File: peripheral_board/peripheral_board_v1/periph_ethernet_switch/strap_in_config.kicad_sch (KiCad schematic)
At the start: 21 parts, among them J10 Conn_01x03, J11 Conn_01x03, J12 Conn_01x03, J6 Conn_01x03, J7 Conn_01x03, J8 Conn_01x03, J9 Conn_01x03

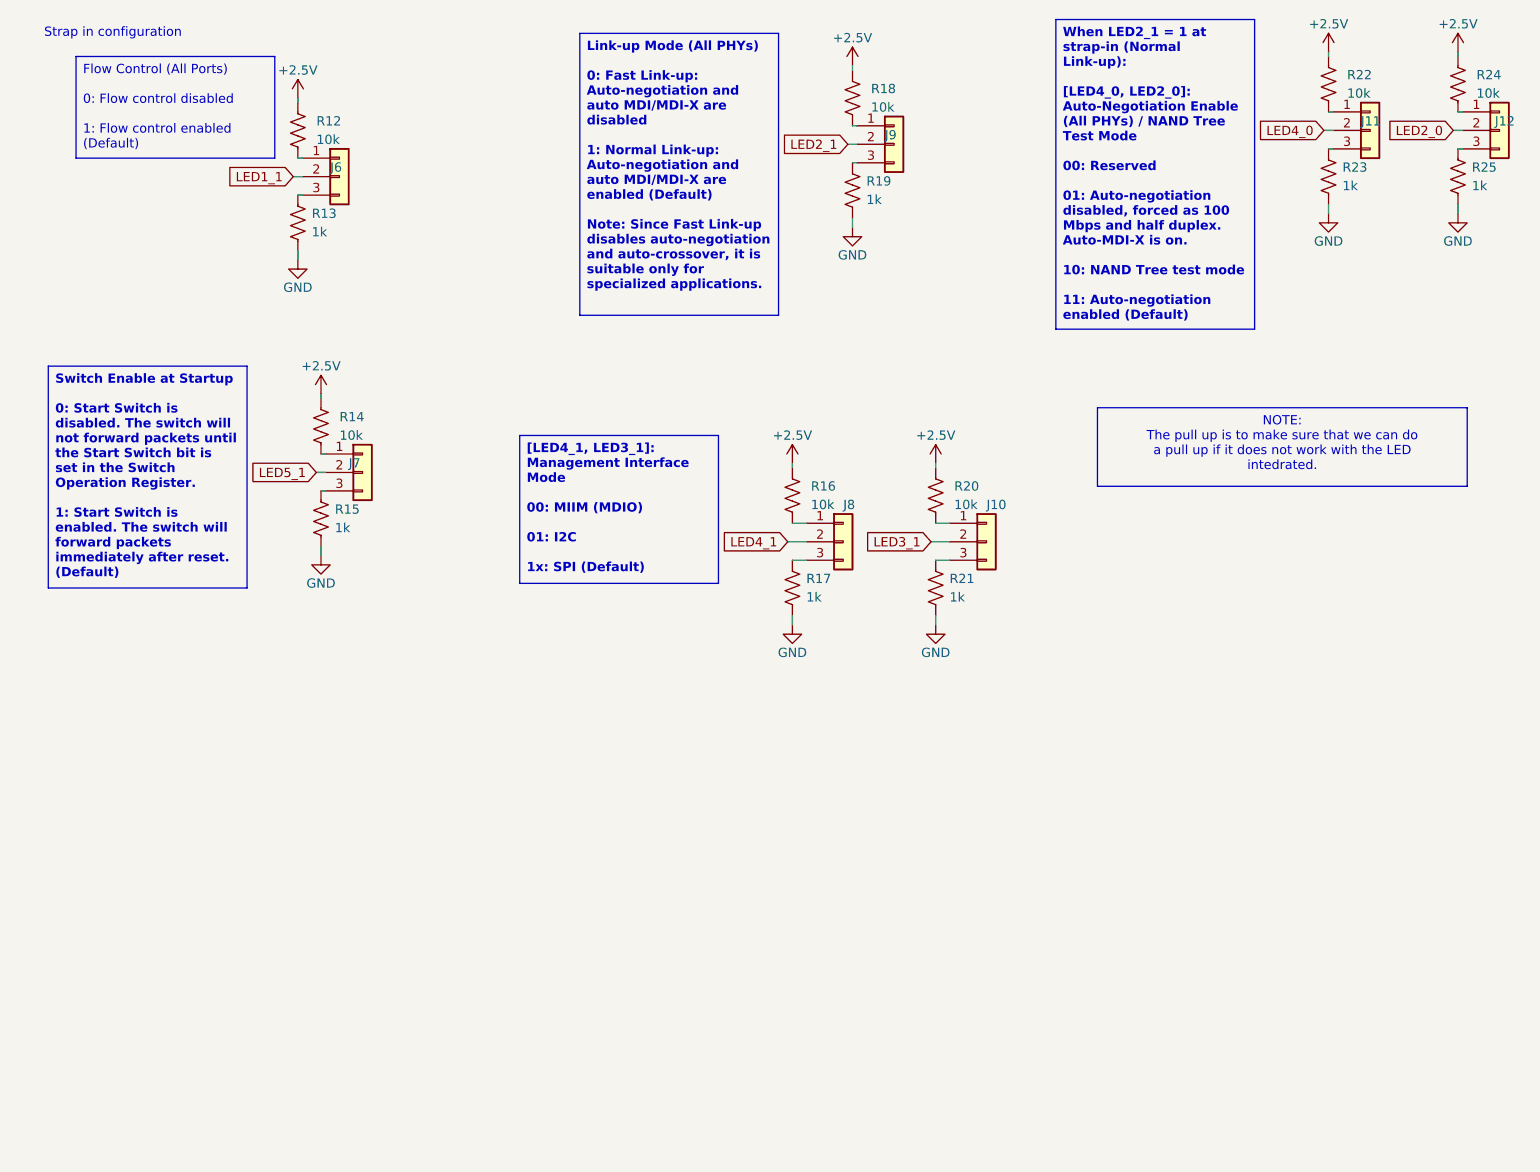
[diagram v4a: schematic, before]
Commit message: Changes based on Microchip support
Made some changes for the strap in configuration. Did some some layout changes. Used the same circuit for the clock and strap in switch from their other Dev kit. Waiting on them to get back to me for a potential schematic review/board review.
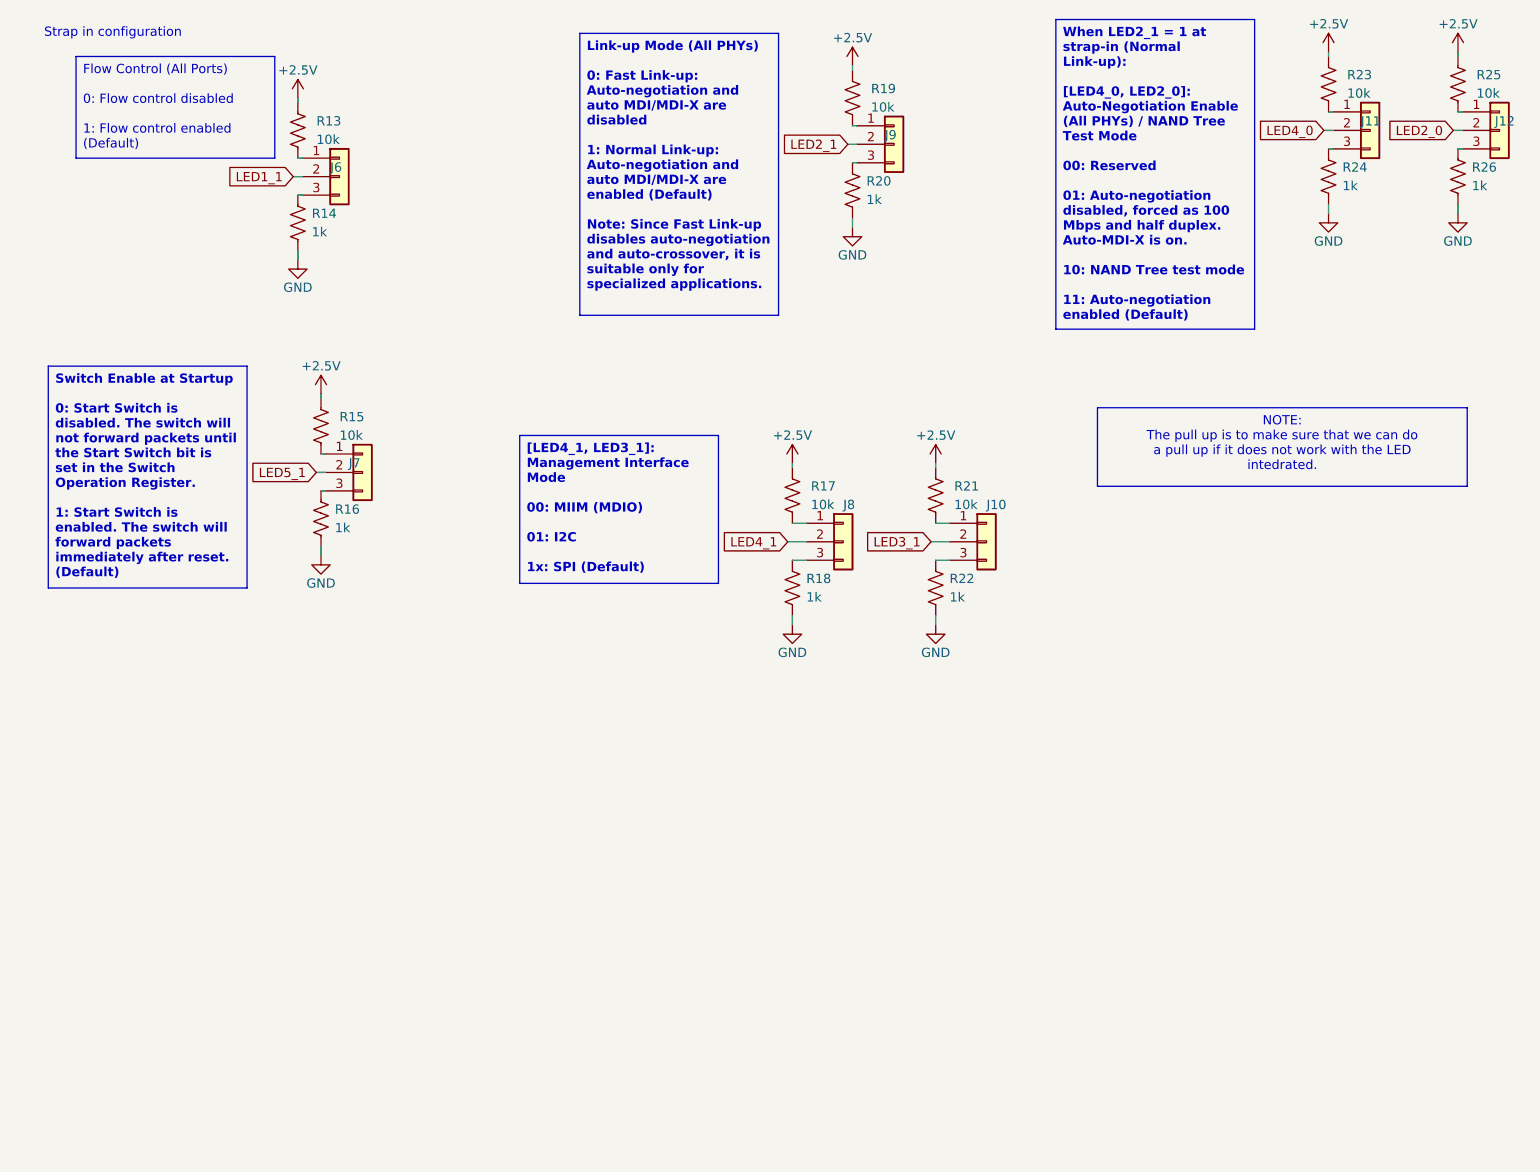
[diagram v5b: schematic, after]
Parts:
- renumbered R12 to R13, R13 to R14, R14 to R15, R15 to R16, R16 to R17, R17 to R18, R18 to R19, R19 to R20, R20 to R21, R21 to R22, R22 to R23, R23 to R24, R24 to R25, R25 to R26
